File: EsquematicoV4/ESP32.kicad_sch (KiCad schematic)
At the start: 11 parts, among them U3 ESP32-WROOM-32

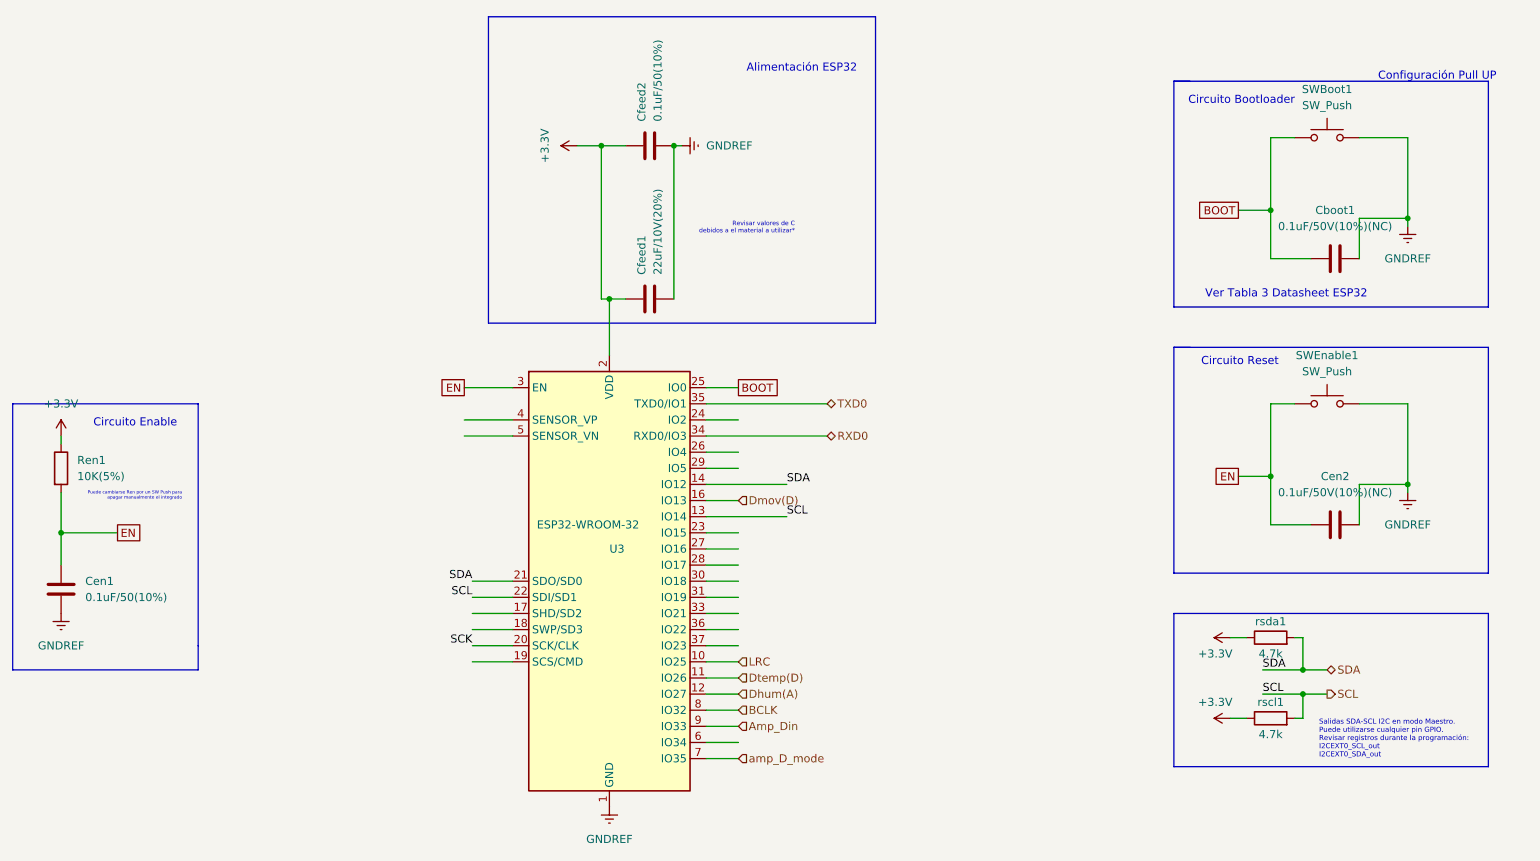
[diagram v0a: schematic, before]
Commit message: Correciones Finales Esquemático - Revisar error con huella del Amplificador de Sonido
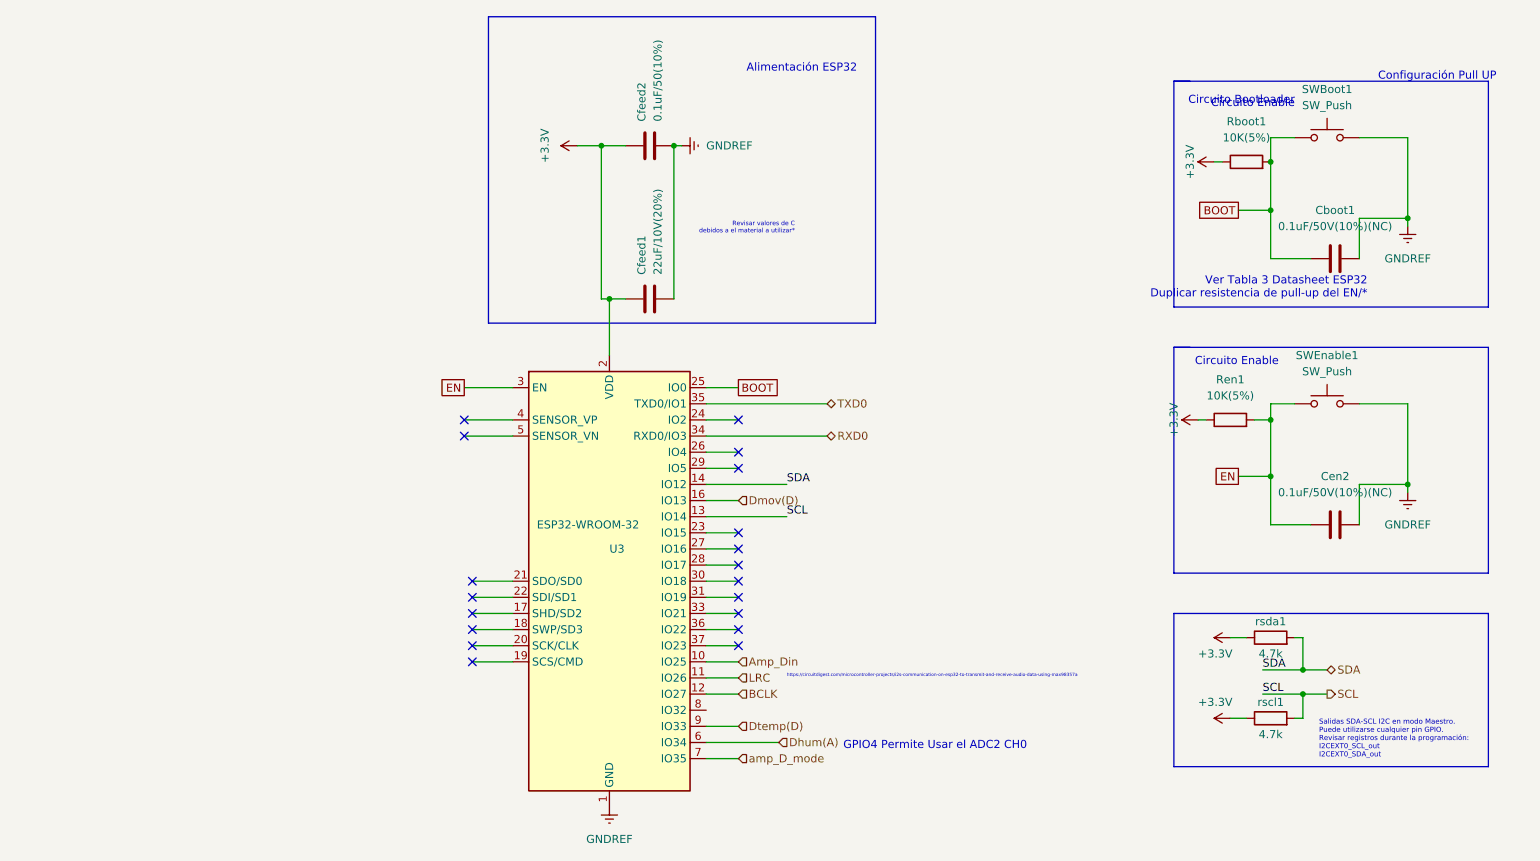
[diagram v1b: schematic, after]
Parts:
- removed Cen1: 0.1uF/50(10%), Capacitor_SMD:C_0805_2012Metric_Pad1.18x1.45mm_HandSolder, symbol Device:C
- added Rboot1: 10K(5%), Resistor_SMD:R_0805_2012Metric_Pad1.20x1.40mm_HandSolder, symbol Device:R
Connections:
- net +3.3V: now also Rboot1.1
- net Amp_Din: now also U3.10 (IO25); no longer U3.9 (IO33)
- net BCLK: now also U3.12 (IO27); no longer U3.8 (IO32)
- net BOOT: now also Rboot1.2
- net Dhum(A): now also U3.6 (IO34); no longer U3.12 (IO27)
- net Dtemp(D): now also U3.9 (IO33); no longer U3.11 (IO26)
- net LRC: now also U3.11 (IO26); no longer U3.10 (IO25)
- net SCL: no longer U3.22 (SDI/SD1)
- net SDA: no longer U3.21 (SDO/SD0)
- net SCK: no longer names the net of U3.20 (SCK/CLK)
- no-connect marks 0 -> 19
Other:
- note added: "GPIO4 Permite Usar el ADC2 CH0"
- note added: "Ver Tabla 3 Datasheet ESP32 Duplicar resistencia de pull-up del EN/*"
- note added: "https://circuitdigest.com/microcontroller-projects/i2s-communication-on-esp32-to-transmit-and-receive-audio-data-using-max98357a"
- note removed: "Circuito Reset"
- note removed: "Puede cambiarse Ren por un SW Push para apagar manualmente el integrado"
- note removed: "Ver Tabla 3 Datasheet ESP32"
